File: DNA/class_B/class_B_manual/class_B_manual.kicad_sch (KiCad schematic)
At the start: 4 parts

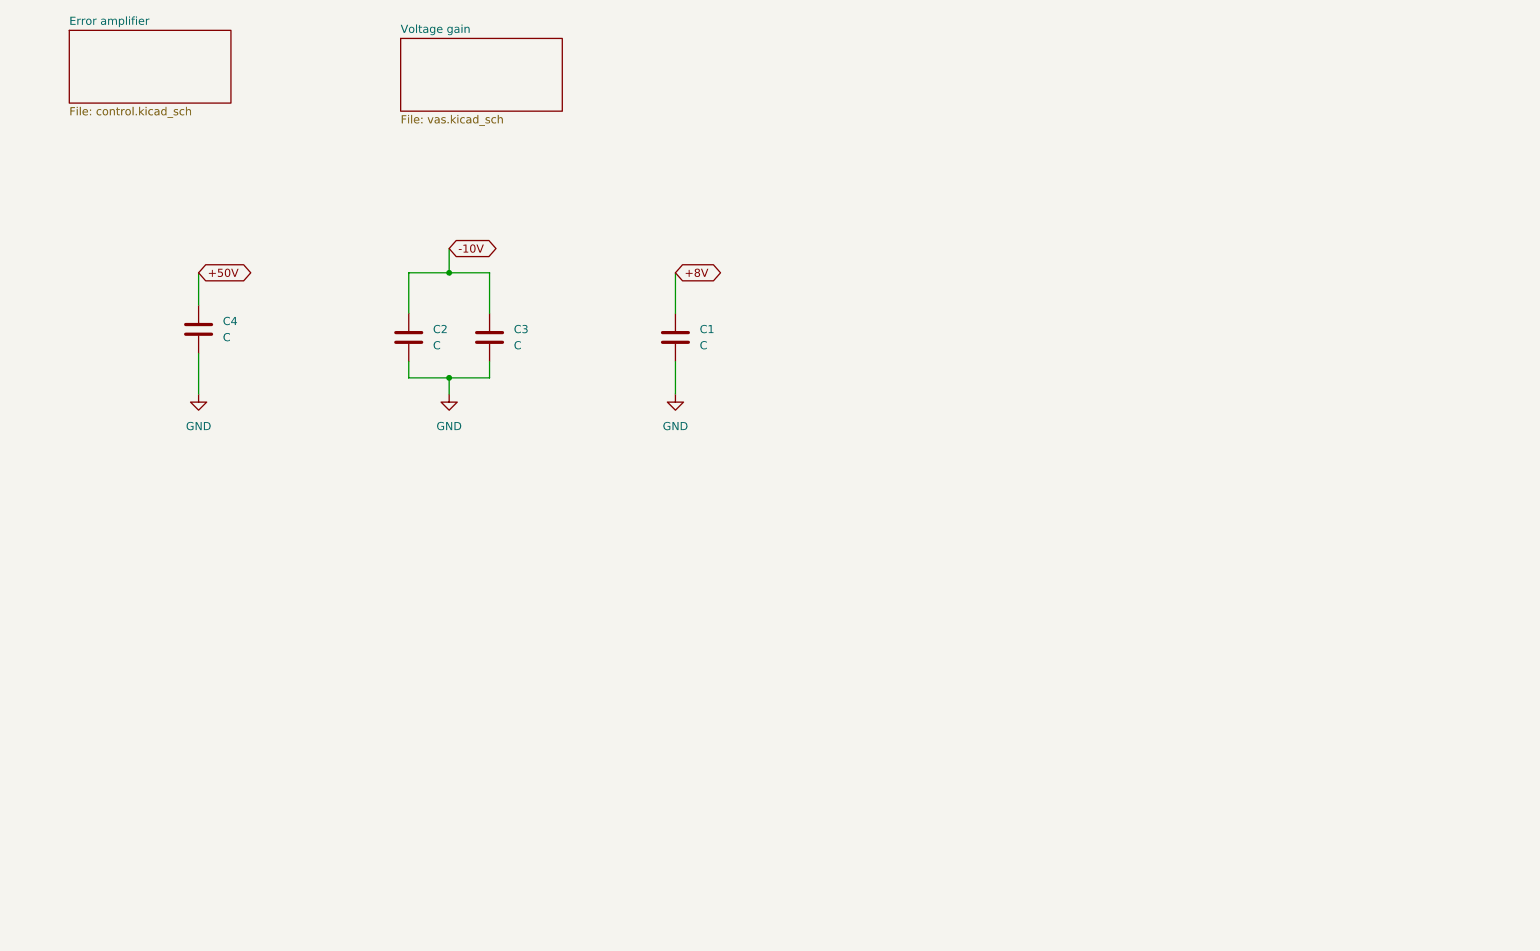
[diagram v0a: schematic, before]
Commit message: [DNA]: all the schematics for Class B amplifier is ready.
TODO: 1. Add resistors', capacitors' values. 2. Add all footprints for resistors and connectors.
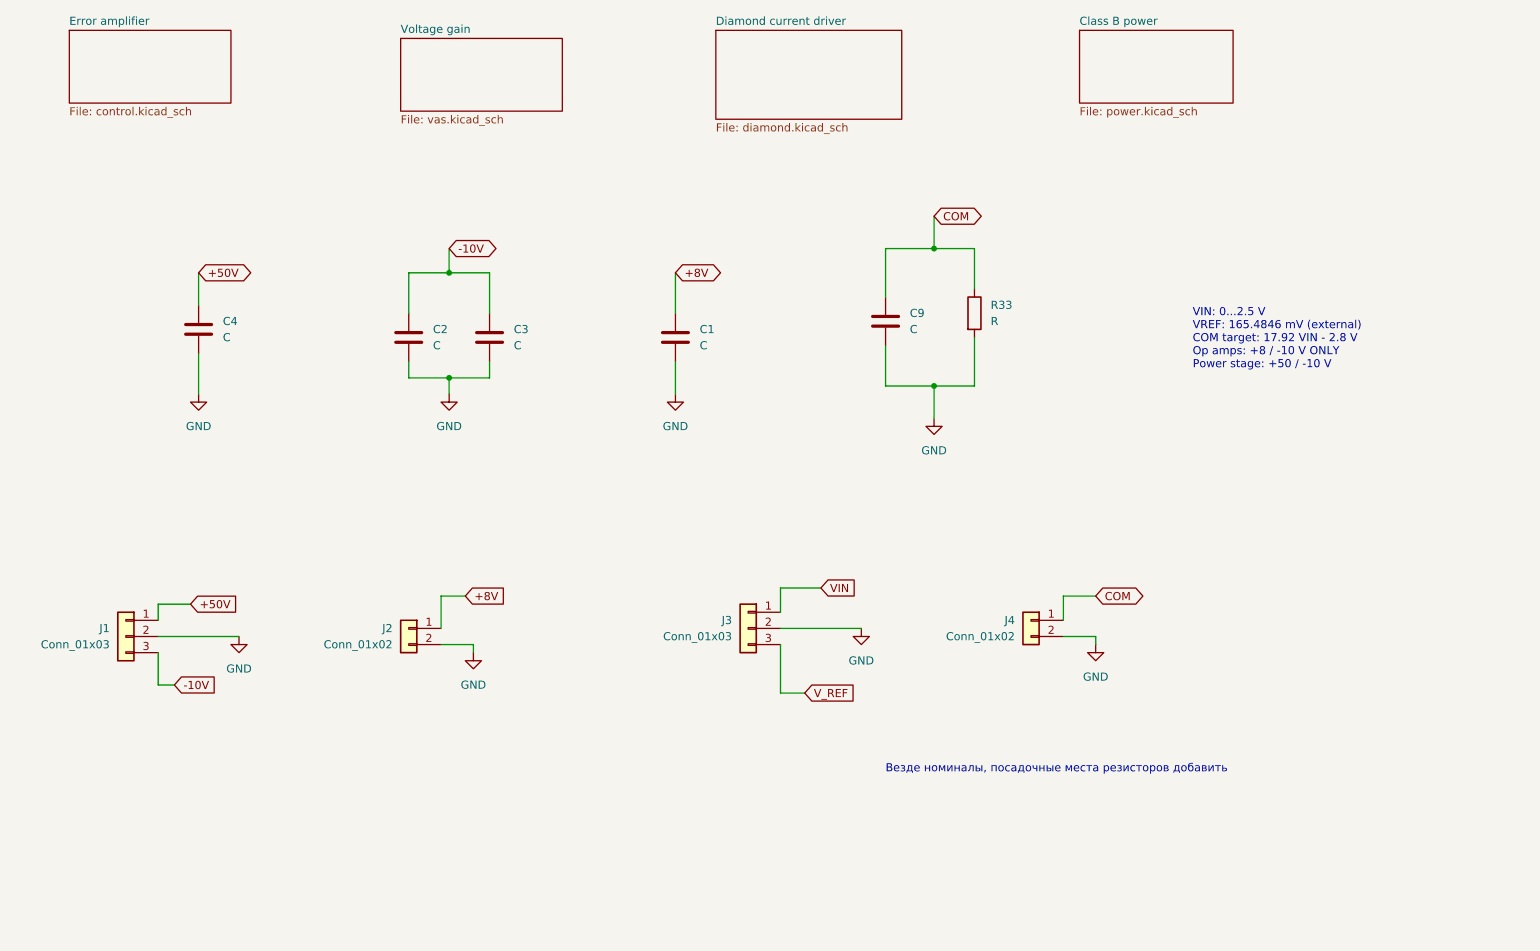
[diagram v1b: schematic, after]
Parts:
- added C9: C, symbol Device:C
- added J1, J3: Conn_01x03, symbol Connector_Generic:Conn_01x03
- added J2, J4: Conn_01x02, symbol Connector_Generic:Conn_01x02
- added R33: R, symbol Device:R
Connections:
- net +50V: now also J1.1 (Pin_1)
- net +8V: now also J2.1 (Pin_1)
- net -10V: now also J1.3 (Pin_3)
- net GND: now also C9.2, J1.2 (Pin_2), J2.2 (Pin_2), J3.2 (Pin_2), J4.2 (Pin_2), R33.2
- new net COM: C9.1, J4.1 (Pin_1), R33.1
- new net VIN: J3.1 (Pin_1)
- new net V_REF: J3.3 (Pin_3)
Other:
- added sheet Class B power (power.kicad_sch)
- added sheet Diamond current driver (diamond.kicad_sch)
- note added: "VIN: 0...2.5 V VREF: 165.4846 mV (external) COM target: 17.92 VIN - 2.8 V Op amps: +8 / -10 V ONLY Power stage: +50 / -10 V"
- note added: "Везде номиналы, посадочные места резисторов добавить"

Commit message: [DNA]: class B: hierarchical labels added.
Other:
- sheet Class B power ports: added COM, DRIVE, OUT_INT; removed none
- sheet Diamond current driver ports: added DRIVE, VAS_OUT; removed none
- sheet Error amplifier ports: added DRIVE, LV_OUT, OUT_INT, VIN, V_REF; removed none
- sheet Voltage gain ports: added LV_OUT, VAS_OUT; removed none
- moved on the sheet: C1, C2, C3, C4, C9, J1, J2, J3, J4, R33

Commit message: [DNA]: class B, resistor values etc added.
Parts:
- C1, C2, C3, C4: value C -> 100n
- C9: value C -> 300n
- R33: value R -> 100k
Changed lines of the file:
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@@
       (effects (font (size 1.27 1.27)) (justify left))
     )
-    (property "Value" "C" (at 87.63 107.95 0)
+    (property "Value" "100n" (at 87.63 107.95 0)
       (effects (font (size 1.27 1.27)) (justify left))
     )
@@
       (effects (font (size 1.27 1.27)) (justify left))
     )
-    (property "Value" "C" (at 129.54 107.95 0)
+    (property "Value" "100n" (at 129.54 107.95 0)
       (effects (font (size 1.27 1.27)) (justify left))
     )
@@
       (effects (font (size 1.27 1.27)) (justify left))
     )
-    (property "Value" "R" (at 175.26 104.14 0)
+    (property "Value" "100k" (at 175.26 104.14 0)
       (effects (font (size 1.27 1.27)) (justify left))
     )
@@
       (effects (font (size 1.27 1.27)) (justify left))
     )
-    (property "Value" "C" (at 162.56 105.41 0)
+    (property "Value" "300n" (at 162.56 105.41 0)
       (effects (font (size 1.27 1.27)) (justify left))
     )
@@
       (effects (font (size 1.27 1.27)) (justify left))
     )
-    (property "Value" "C" (at 54.61 106.68 0)
+    (property "Value" "100n" (at 54.61 106.68 0)
       (effects (font (size 1.27 1.27)) (justify left))
     )
@@
       (effects (font (size 1.27 1.27)) (justify left))
     )
-    (property "Value" "C" (at 100.33 107.95 0)
-      (effects (font (size 1.27 1.27)) (justify left))
-    )
+    (property "Value" "100n" (at 100.33 107.95 0)
+      (effects (font (size 1.27 1.27)) (justify left))
+    )
